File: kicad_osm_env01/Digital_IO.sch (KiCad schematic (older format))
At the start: 4 parts

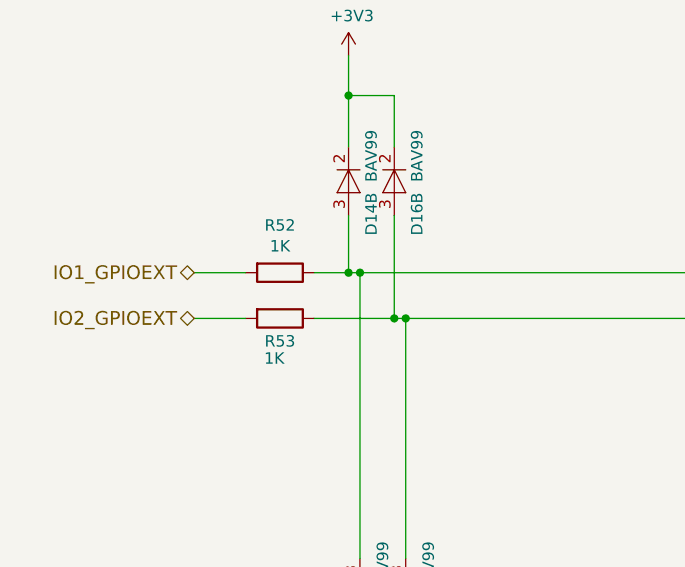
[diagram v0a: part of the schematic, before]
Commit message: pushed latest schematics got started with micro into schematic
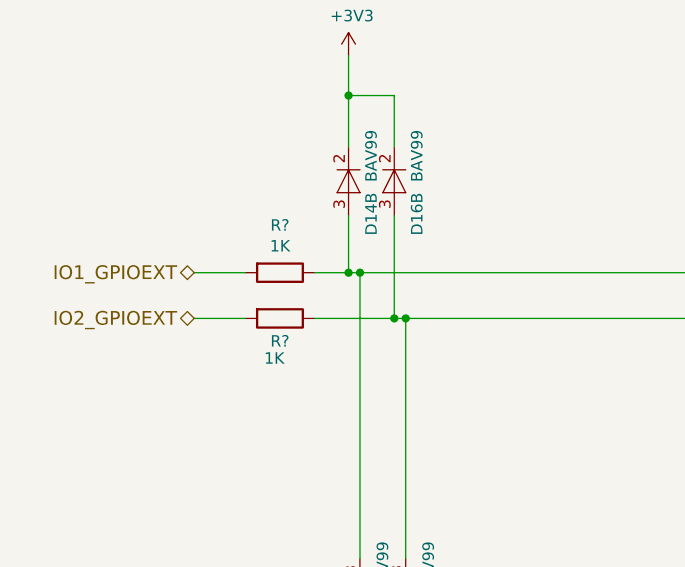
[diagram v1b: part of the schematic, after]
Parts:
- renumbered R52 to R?, R53 to R?
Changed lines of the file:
@@
 $Descr A3 16535 11693
 encoding utf-8
-Sheet 3 4
+Sheet 3 8
 Title "Open Smart Monitor"
 Date ""
@@
 AR Path="/5E6992BF/5C6F6973" Ref="D?"  Part="1"
 AR Path="/5E256652/5C6F6973" Ref="D16"  Part="2"
-F 0 "D16" H 4050 3375 50  0000 L CNN
+F 0 "D?" H 4050 3375 50  0000 L CNN
 F 1 "BAV99" H 3775 3375 50  0000 L CNN
 F 2 "Package_TO_SOT_SMD:SOT-23" H 4000 3125 50  0001 C CNN
@@
 AR Path="/5E6992BF/5C6F6981" Ref="D?"  Part="1"
 AR Path="/5E256652/5C6F6981" Ref="D16"  Part="1"
-F 0 "D16" H 4125 5175 50  0000 L CNN
+F 0 "D?" H 4125 5175 50  0000 L CNN
 F 1 "BAV99" H 3825 5175 50  0000 L CNN
 F 2 "Package_TO_SOT_SMD:SOT-23" H 4050 4925 50  0001 C CNN
@@
 AR Path="/5E6992BF/5C6F69AD" Ref="D?"  Part="1"
 AR Path="/5E256652/5C6F69AD" Ref="D14"  Part="1"
-F 0 "D14" H 3925 5175 50  0000 L CNN
+F 0 "D?" H 3925 5175 50  0000 L CNN
 F 1 "BAV99" H 3625 5175 50  0000 L CNN
 F 2 "Package_TO_SOT_SMD:SOT-23" H 3850 4925 50  0001 C CNN
@@
 AR Path="/5E6992BF/5C6F69B4" Ref="D?"  Part="1"
 AR Path="/5E256652/5C6F69B4" Ref="D14"  Part="2"
-F 0 "D14" H 3850 3375 50  0000 L CNN
+F 0 "D?" H 3850 3375 50  0000 L CNN
 F 1 "BAV99" H 3575 3375 50  0000 L CNN
 F 2 "Package_TO_SOT_SMD:SOT-23" H 3800 3125 50  0001 C CNN
@@
 AR Path="/5E6992BF/5C72E068" Ref="#PWR?"  Part="1"
 AR Path="/5E256652/5C72E068" Ref="#PWR0194"  Part="1"
-F 0 "#PWR0194" H 3800 2575 50  0001 C CNN
+F 0 "#PWR?" H 3800 2575 50  0001 C CNN
 F 1 "+3V3" H 3815 2898 50  0000 C CNN
 F 2 "" H 3800 2725 50  0001 C CNN
@@
 	4050 3875 5875 3875
 $Comp
-L OSM_env01-rescue:R-device-ESP32-EVB_Rev_D-rescue R52
+L OSM_env01-rescue:R-device-ESP32-EVB_Rev_D-rescue R?
 U 1 1 5E0C2504
 P 3500 3675
-F 0 "R52" V 3293 3675 50  0000 C CNN
+F 0 "R?" V 3293 3675 50  0000 C CNN
 F 1 "1K" V 3384 3675 50  0000 C CNN
 F 2 "Resistor_SMD:R_0603_1608Metric" V 3430 3675 50  0001 C CNN
@@
 $EndComp
 $Comp
-L OSM_env01-rescue:R-device-ESP32-EVB_Rev_D-rescue R53
+L OSM_env01-rescue:R-device-ESP32-EVB_Rev_D-rescue R?
 U 1 1 5E0C53CF
 P 3500 3875
-F 0 "R53" V 3600 3875 50  0000 C CNN
+F 0 "R?" V 3600 3875 50  0000 C CNN
 F 1 "1K" V 3675 3850 50  0000 C CNN
 F 2 "Resistor_SMD:R_0603_1608Metric" V 3430 3875 50  0001 C CNN

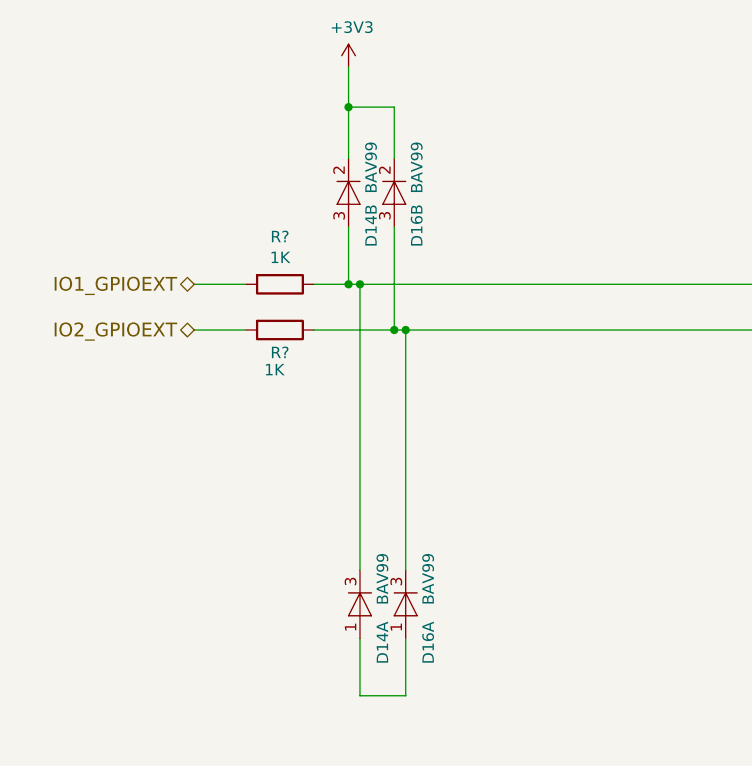
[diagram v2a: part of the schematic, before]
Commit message: updated schematics
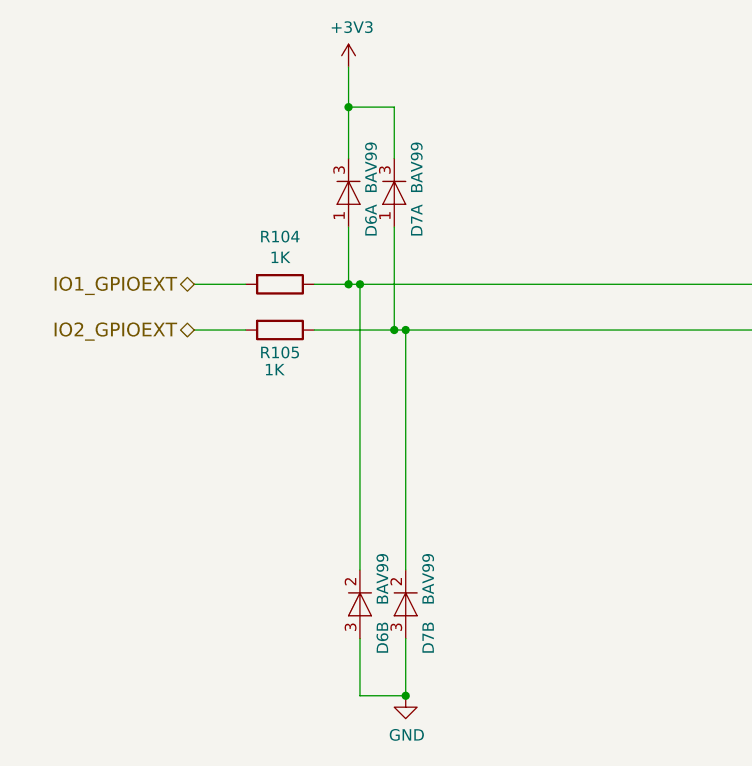
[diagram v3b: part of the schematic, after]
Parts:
- gave numbers to parts that had none: 2
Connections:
- net +3V3: now also D14.3 (K), D16.3 (K); no longer D14.2 (K), D16.2 (K)
- net IO1_GPIOINT: now also D14.1 (A), D14.2 (K); no longer D14.3 (A), D14.3 (K)
- net IO2_GPIOINT: now also D16.1 (A), D16.2 (K); no longer D16.3 (A), D16.3 (K)
- new net GND: D14.3 (A), D16.3 (A)
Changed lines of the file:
@@
 $Descr A3 16535 11693
 encoding utf-8
-Sheet 3 9
+Sheet 8 11
 Title "Open Smart Monitor"
 Date ""
@@
 	3800 2725 3800 2900
 Wire Wire Line
-	3850 5475 4050 5475
-Wire Wire Line
 	3850 5225 3850 5475
 Wire Wire Line
@@
 $Comp
 L OSM_env01-rescue:BAV99-Diode-ESP32-EVB_Rev_D-rescue D16
-U 2 1 5C6F6973
+U 1 1 5C6F6973
 P 4000 3275
 AR Path="/5C358B39/5C6F6973" Ref="D16"  Part="2"
 AR Path="/5E6992BF/5C6F6973" Ref="D?"  Part="1"
 AR Path="/5E256652/5C6F6973" Ref="D16"  Part="2"
-AR Path="/608F4675/60920857/5C6F6973" Ref="D?"  Part="2"
-F 0 "D?" H 4050 3375 50  0000 L CNN
+AR Path="/608F4675/60920857/5C6F6973" Ref="D7"  Part="1"
+F 0 "D7" H 4050 3375 50  0000 L CNN
 F 1 "BAV99" H 3775 3375 50  0000 L CNN
 F 2 "Package_TO_SOT_SMD:SOT-23" H 4000 3125 50  0001 C CNN
 F 3 "www.nxp.com/documents/data_sheet/BAV99_SER.pdf" H 4000 3375 50  0001 C CNN
 F 4 "134-001" H 4000 3275 50  0001 C CNN "Devtank"
-	2    4000 3275
+	1    4000 3275
 	0    1    1    0
 $EndComp
 $Comp
 L OSM_env01-rescue:BAV99-Diode-ESP32-EVB_Rev_D-rescue D16
-U 1 1 5C6F6981
+U 2 1 5C6F6981
 P 4050 5075
 AR Path="/5C358B39/5C6F6981" Ref="D16"  Part="1"
 AR Path="/5E6992BF/5C6F6981" Ref="D?"  Part="1"
 AR Path="/5E256652/5C6F6981" Ref="D16"  Part="1"
-AR Path="/608F4675/60920857/5C6F6981" Ref="D?"  Part="1"
-F 0 "D?" H 4125 5175 50  0000 L CNN
+AR Path="/608F4675/60920857/5C6F6981" Ref="D7"  Part="2"
+F 0 "D7" H 4125 5175 50  0000 L CNN
 F 1 "BAV99" H 3825 5175 50  0000 L CNN
 F 2 "Package_TO_SOT_SMD:SOT-23" H 4050 4925 50  0001 C CNN
 F 3 "www.nxp.com/documents/data_sheet/BAV99_SER.pdf" H 4050 5175 50  0001 C CNN
 F 4 "134-001" H 4050 5075 50  0001 C CNN "Devtank"
-	1    4050 5075
+	2    4050 5075
 	0    1    1    0
 $EndComp
@@
 $Comp
 L OSM_env01-rescue:BAV99-Diode-ESP32-EVB_Rev_D-rescue D14
-U 1 1 5C6F69AD
+U 2 1 5C6F69AD
 P 3850 5075
 AR Path="/5C358B39/5C6F69AD" Ref="D14"  Part="1"
 AR Path="/5E6992BF/5C6F69AD" Ref="D?"  Part="1"
 AR Path="/5E256652/5C6F69AD" Ref="D14"  Part="1"
-AR Path="/608F4675/60920857/5C6F69AD" Ref="D?"  Part="1"
-F 0 "D?" H 3925 5175 50  0000 L CNN
+AR Path="/608F4675/60920857/5C6F69AD" Ref="D6"  Part="2"
+F 0 "D6" H 3925 5175 50  0000 L CNN
 F 1 "BAV99" H 3625 5175 50  0000 L CNN
 F 2 "Package_TO_SOT_SMD:SOT-23" H 3850 4925 50  0001 C CNN
 F 3 "www.nxp.com/documents/data_sheet/BAV99_SER.pdf" H 3850 5175 50  0001 C CNN
 F 4 "134-001" H 3850 5075 50  0001 C CNN "Devtank"
-	1    3850 5075
+	2    3850 5075
 	0    1    1    0
 $EndComp
 $Comp
 L OSM_env01-rescue:BAV99-Diode-ESP32-EVB_Rev_D-rescue D14
-U 2 1 5C6F69B4
+U 1 1 5C6F69B4
 P 3800 3275
 AR Path="/5C358B39/5C6F69B4" Ref="D14"  Part="2"
 AR Path="/5E6992BF/5C6F69B4" Ref="D?"  Part="1"
 AR Path="/5E256652/5C6F69B4" Ref="D14"  Part="2"
-AR Path="/608F4675/60920857/5C6F69B4" Ref="D?"  Part="2"
-F 0 "D?" H 3850 3375 50  0000 L CNN
+AR Path="/608F4675/60920857/5C6F69B4" Ref="D6"  Part="1"
+F 0 "D6" H 3850 3375 50  0000 L CNN
 F 1 "BAV99" H 3575 3375 50  0000 L CNN
 F 2 "Package_TO_SOT_SMD:SOT-23" H 3800 3125 50  0001 C CNN
 F 3 "www.nxp.com/documents/data_sheet/BAV99_SER.pdf" H 3800 3375 50  0001 C CNN
 F 4 "134-001" H 3800 3275 50  0001 C CNN "Devtank"
-	2    3800 3275
+	1    3800 3275
 	0    1    1    0
 $EndComp
@@
 AR Path="/5E6992BF/5C72E068" Ref="#PWR?"  Part="1"
 AR Path="/5E256652/5C72E068" Ref="#PWR0194"  Part="1"
-AR Path="/608F4675/60920857/5C72E068" Ref="#PWR?"  Part="1"
-F 0 "#PWR?" H 3800 2575 50  0001 C CNN
+AR Path="/608F4675/60920857/5C72E068" Ref="#PWR093"  Part="1"
+F 0 "#PWR093" H 3800 2575 50  0001 C CNN
 F 1 "+3V3" H 3815 2898 50  0000 C CNN
 F 2 "" H 3800 2725 50  0001 C CNN
@@
 	4050 3875 5875 3875
 $Comp
-L OSM_env01-rescue:R-device-ESP32-EVB_Rev_D-rescue R?
+L OSM_env01-rescue:R-device-ESP32-EVB_Rev_D-rescue R104
 U 1 1 5E0C2504
 P 3500 3675
-F 0 "R?" V 3293 3675 50  0000 C CNN
+F 0 "R104" V 3293 3675 50  0000 C CNN
 F 1 "1K" V 3384 3675 50  0000 C CNN
 F 2 "Resistor_SMD:R_0603_1608Metric" V 3430 3675 50  0001 C CNN
@@
 $EndComp
 $Comp
-L OSM_env01-rescue:R-device-ESP32-EVB_Rev_D-rescue R?
+L OSM_env01-rescue:R-device-ESP32-EVB_Rev_D-rescue R105
 U 1 1 5E0C53CF
 P 3500 3875
-F 0 "R?" V 3600 3875 50  0000 C CNN
+F 0 "R105" V 3600 3875 50  0000 C CNN
 F 1 "1K" V 3675 3850 50  0000 C CNN
 F 2 "Resistor_SMD:R_0603_1608Metric" V 3430 3875 50  0001 C CNN
@@
 	0    1    1    0
 $EndComp
+$Comp
+L OSM_env01:GND #PWR0128
+U 1 1 614EEF04
+P 4050 5475
+F 0 "#PWR0128" H 4050 5225 50  0001 C CNN
+F 1 "GND" H 4055 5302 50  0000 C CNN
+F 2 "" H 4050 5475 60  0000 C CNN
+F 3 "" H 4050 5475 60  0000 C CNN
+	1    4050 5475
+	1    0    0    -1
+$EndComp
+Connection ~ 4050 5475
+Wire Wire Line
+	3850 5475 4050 5475
 $EndSCHEMATC

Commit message: schematics awaiting review
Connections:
- net +3V3: now also D14.2 (K), D16.2 (K); no longer D14.3 (K), D16.3 (K)
- net GND: now also D14.1 (A), D16.1 (A); no longer D14.3 (A), D16.3 (A)
- net IO1_GPIOINT: now also D14.3 (A), D14.3 (K); no longer D14.1 (A), D14.2 (K)
- net IO2_GPIOINT: now also D16.3 (A), D16.3 (K); no longer D16.1 (A), D16.2 (K)
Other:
- moved on the sheet: D6A, D6B, D7A, D7B
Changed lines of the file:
@@
 L OSM_env01-rescue:BAV99-Diode-ESP32-EVB_Rev_D-rescue D16
 U 1 1 5C6F6973
-P 4000 3275
+P 4050 5075
 AR Path="/5C358B39/5C6F6973" Ref="D16"  Part="2"
 AR Path="/5E6992BF/5C6F6973" Ref="D?"  Part="1"
 AR Path="/5E256652/5C6F6973" Ref="D16"  Part="2"
 AR Path="/608F4675/60920857/5C6F6973" Ref="D7"  Part="1"
-F 0 "D7" H 4050 3375 50  0000 L CNN
-F 1 "BAV99" H 3775 3375 50  0000 L CNN
-F 2 "Package_TO_SOT_SMD:SOT-23" H 4000 3125 50  0001 C CNN
-F 3 "www.nxp.com/documents/data_sheet/BAV99_SER.pdf" H 4000 3375 50  0001 C CNN
-F 4 "134-001" H 4000 3275 50  0001 C CNN "Devtank"
-	1    4000 3275
+F 0 "D7" H 4100 5175 50  0000 L CNN
+F 1 "BAV99" H 3825 5175 50  0000 L CNN
+F 2 "Package_TO_SOT_SMD:SOT-23" H 4050 4925 50  0001 C CNN
+F 3 "www.nxp.com/documents/data_sheet/BAV99_SER.pdf" H 4050 5175 50  0001 C CNN
+F 4 "134-001" H 4050 5075 50  0001 C CNN "Devtank"
+	1    4050 5075
 	0    1    1    0
 $EndComp
@@
 L OSM_env01-rescue:BAV99-Diode-ESP32-EVB_Rev_D-rescue D16
 U 2 1 5C6F6981
-P 4050 5075
+P 4000 3275
 AR Path="/5C358B39/5C6F6981" Ref="D16"  Part="1"
 AR Path="/5E6992BF/5C6F6981" Ref="D?"  Part="1"
 AR Path="/5E256652/5C6F6981" Ref="D16"  Part="1"
 AR Path="/608F4675/60920857/5C6F6981" Ref="D7"  Part="2"
-F 0 "D7" H 4125 5175 50  0000 L CNN
-F 1 "BAV99" H 3825 5175 50  0000 L CNN
-F 2 "Package_TO_SOT_SMD:SOT-23" H 4050 4925 50  0001 C CNN
-F 3 "www.nxp.com/documents/data_sheet/BAV99_SER.pdf" H 4050 5175 50  0001 C CNN
-F 4 "134-001" H 4050 5075 50  0001 C CNN "Devtank"
-	2    4050 5075
+F 0 "D7" H 4075 3375 50  0000 L CNN
+F 1 "BAV99" H 3775 3375 50  0000 L CNN
+F 2 "Package_TO_SOT_SMD:SOT-23" H 4000 3125 50  0001 C CNN
+F 3 "www.nxp.com/documents/data_sheet/BAV99_SER.pdf" H 4000 3375 50  0001 C CNN
+F 4 "134-001" H 4000 3275 50  0001 C CNN "Devtank"
+	2    4000 3275
 	0    1    1    0
 $EndComp
@@
 L OSM_env01-rescue:BAV99-Diode-ESP32-EVB_Rev_D-rescue D14
 U 2 1 5C6F69AD
-P 3850 5075
+P 3800 3275
 AR Path="/5C358B39/5C6F69AD" Ref="D14"  Part="1"
 AR Path="/5E6992BF/5C6F69AD" Ref="D?"  Part="1"
 AR Path="/5E256652/5C6F69AD" Ref="D14"  Part="1"
 AR Path="/608F4675/60920857/5C6F69AD" Ref="D6"  Part="2"
-F 0 "D6" H 3925 5175 50  0000 L CNN
-F 1 "BAV99" H 3625 5175 50  0000 L CNN
-F 2 "Package_TO_SOT_SMD:SOT-23" H 3850 4925 50  0001 C CNN
-F 3 "www.nxp.com/documents/data_sheet/BAV99_SER.pdf" H 3850 5175 50  0001 C CNN
-F 4 "134-001" H 3850 5075 50  0001 C CNN "Devtank"
-	2    3850 5075
+F 0 "D6" H 3875 3375 50  0000 L CNN
+F 1 "BAV99" H 3575 3375 50  0000 L CNN
+F 2 "Package_TO_SOT_SMD:SOT-23" H 3800 3125 50  0001 C CNN
+F 3 "www.nxp.com/documents/data_sheet/BAV99_SER.pdf" H 3800 3375 50  0001 C CNN
+F 4 "134-001" H 3800 3275 50  0001 C CNN "Devtank"
+	2    3800 3275
 	0    1    1    0
 $EndComp
@@
 L OSM_env01-rescue:BAV99-Diode-ESP32-EVB_Rev_D-rescue D14
 U 1 1 5C6F69B4
-P 3800 3275
+P 3850 5075
 AR Path="/5C358B39/5C6F69B4" Ref="D14"  Part="2"
 AR Path="/5E6992BF/5C6F69B4" Ref="D?"  Part="1"
 AR Path="/5E256652/5C6F69B4" Ref="D14"  Part="2"
 AR Path="/608F4675/60920857/5C6F69B4" Ref="D6"  Part="1"
-F 0 "D6" H 3850 3375 50  0000 L CNN
-F 1 "BAV99" H 3575 3375 50  0000 L CNN
-F 2 "Package_TO_SOT_SMD:SOT-23" H 3800 3125 50  0001 C CNN
-F 3 "www.nxp.com/documents/data_sheet/BAV99_SER.pdf" H 3800 3375 50  0001 C CNN
-F 4 "134-001" H 3800 3275 50  0001 C CNN "Devtank"
-	1    3800 3275
+F 0 "D6" H 3900 5175 50  0000 L CNN
+F 1 "BAV99" H 3625 5175 50  0000 L CNN
+F 2 "Package_TO_SOT_SMD:SOT-23" H 3850 4925 50  0001 C CNN
+F 3 "www.nxp.com/documents/data_sheet/BAV99_SER.pdf" H 3850 5175 50  0001 C CNN
+F 4 "134-001" H 3850 5075 50  0001 C CNN "Devtank"
+	1    3850 5075
 	0    1    1    0
 $EndComp
